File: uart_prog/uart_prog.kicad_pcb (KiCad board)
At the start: 2 copper layers, 22 parts, among them J1 USB_B_Micro, J2 Conn_01x06, Q1 MBT3904DW1, SW1 SW_SPDT, U1 FT231XQ

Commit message: Add pcb
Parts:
- moved R5 30.6 mm to (142.0, 80.0), turned to 180 degrees
- moved TP1 26.2 mm to (151.5, 77.5)
- moved TP2 25.7 mm to (156.5, 77.5)
- moved D1 23.5 mm to (146.3, 80.0), turned to 180 degrees
- moved R6 21.0 mm to (142.0, 77.5), turned to 180 degrees
- moved Q1 20.1 mm to (154.0, 82.0), turned to 270 degrees
- moved D2 19.2 mm to (146.3, 77.5), turned to 180 degrees
- moved C4 18.7 mm to (146.5, 85.0), turned to 180 degrees
- moved R3 17.6 mm to (151.5, 81.9), turned to 270 degrees
- moved R4 16.0 mm to (156.5, 81.9), turned to 90 degrees
- moved C5 14.0 mm to (153.1, 91.5)
- moved J2 11.3 mm to (167.0, 78.5)
- moved FB1 2.00 mm to (146.5, 83.0)
- moved F1 1.50 mm to (142.0, 83.0)

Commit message: Layout doner
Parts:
- removed TP1, TP2: TestPoint, TestPoint:TestPoint_THTPad_D2.0mm_Drill1.0mm
- C3: footprint Capacitor_SMD:C_01005_0402Metric -> Capacitor_SMD:C_0805_2012Metric_Pad1.18x1.45mm_HandSolder
- SW1: moved to B.Cu
- moved C3 19.9 mm to (146.5, 84.2)
- moved C4 10.9 mm to (157.0, 87.9), turned to 90 degrees
- moved C5 7.91 mm to (150.6, 84.0), turned to 180 degrees
- moved J2 6.75 mm to (160.2, 78.8)
- moved R3 6.21 mm to (157.6, 80.5), turned to 90 degrees
- moved R4 4.19 mm to (152.6, 80.5), turned to 270 degrees
- moved R5 2.37 mm to (142.7, 77.8)
- moved R6 2.37 mm to (142.7, 79.8)
- moved D2 2.27 mm to (146.5, 79.8)
- moved D1 2.26 mm to (146.5, 77.8)
- moved Q1 1.96 mm to (155.1, 80.3), turned to 90 degrees
- moved J1 1.75 mm to (136.8, 89.0)
- moved C1 1.58 mm to (143.5, 91.4)
- moved C2 1.58 mm to (143.5, 88.1)
- moved R1 1.58 mm to (146.1, 90.5)
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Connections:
- J1 pad 4: (no net) -> Net-(J1-Pad4)
- J2 pad 1: rx -> EN
- J2 pad 2: tx -> BOOT_OPT
- J2 pad 3: EN -> rx
- J2 pad 4: BOOT_OPT -> tx
- U1 pad 15: (no net) -> Net-(U1-Pad15)
- U1 pad 16: (no net) -> Net-(U1-Pad16)
- U1 pad 2: (no net) -> Net-(U1-Pad2)
- U1 pad 4: (no net) -> Net-(U1-Pad4)
- U1 pad 5: (no net) -> Net-(U1-Pad5)
- U1 pad 6: (no net) -> Net-(U1-Pad6)
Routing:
- net 5v: track 0.00 -> 36.5 mm, vias 0 -> 2
- net 3v3: track 0.00 -> 33.9 mm, vias 0 -> 2
- net vccio: track 0.00 -> 33.1 mm, vias 0 -> 2
- net GND: track 0.00 -> 27.3 mm, vias 0 -> 2
- net rxled: track 0.00 -> 20.4 mm, vias 0 -> 2
- net txled: track 0.00 -> 16.3 mm, vias 0 -> 2
- net rx: track 0.00 -> 15.0 mm, vias 0 -> 2
- net dtr: track 0.00 -> 14.6 mm, vias 0 -> 2
- net Net-(F1-Pad1): track 0.00 -> 8.41 mm, vias 0 -> 2
- net rts: track 0.00 -> 7.90 mm, vias 0 -> 2
- net tx: track 0.00 -> 7.73 mm
- net EN: track 0.00 -> 7.47 mm
- net /in2-: track 6.39 -> 12.4 mm
- net BOOT_OPT: track 0.00 -> 5.78 mm
- net /in2+: track 6.23 -> 11.2 mm
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- added copper zone on B.Cu, net GND
- added copper zone on F.Cu, net GND
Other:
- board outline added: 26.8 x 18.8 mm

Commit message: Pcb rev1
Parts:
- J1, J2: moved to B.Cu
- moved J2 12.8 mm to (160.2, 91.5)
- moved C1 3.54 mm to (143.0, 87.9), turned to 90 degrees
- moved C2 3.04 mm to (143.0, 91.1), turned to 270 degrees
- moved R1 1.90 mm to (145.4, 88.8)
- moved R2 1.46 mm to (145.4, 90.2)
- turned J1 to 90 degrees
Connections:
- J1 pad 4: Net-(J1-Pad4) -> (no net)
- J2 pad 1: EN -> GND
- J2 pad 2: BOOT_OPT -> 5v
- J2 pad 3: rx -> tx
- J2 pad 4: tx -> rx
- J2 pad 5: 5v -> BOOT_OPT
- J2 pad 6: GND -> EN
- U1 pad 15: Net-(U1-Pad15) -> (no net)
- U1 pad 16: Net-(U1-Pad16) -> (no net)
- U1 pad 2: Net-(U1-Pad2) -> (no net)
- U1 pad 4: Net-(U1-Pad4) -> (no net)
- U1 pad 5: Net-(U1-Pad5) -> (no net)
- U1 pad 6: Net-(U1-Pad6) -> (no net)
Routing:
- net Net-(F1-Pad1): track 8.41 -> 11.7 mm, vias 2 -> 1
- net /in2-: track 12.4 -> 9.76 mm, vias 2 -> 0
- net /in2+: track 11.2 -> 9.45 mm, vias 2 -> 0
- net vccio: track 33.1 -> 34.5 mm
- net /in+: track 6.99 -> 5.64 mm, vias 0 -> 1
- net dtr: track 14.6 -> 15.7 mm
- net 3v3: track 33.9 -> 33.1 mm
- net 5v: track 36.5 -> 37.3 mm
- net /in-: track 6.55 -> 5.78 mm, vias 0 -> 1
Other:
- board size 26.8 x 18.8 mm -> 26.8 x 17.5 mm
- board text added: "3v3"
- board text added: "5v"
- board text added: "EN BOOT RX TX 5V GND"

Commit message: Add schematic back again ...
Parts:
- D1, D2: footprint LED_SMD:LED_0805_2012Metric_Pad1.15x1.40mm_HandSolder -> LED_SMD:LED_0603_1608Metric_Pad1.05x0.95mm_HandSolder
- R5, R6: footprint Resistor_SMD:R_0805_2012Metric_Pad1.15x1.40mm_HandSolder -> Resistor_SMD:R_0603_1608Metric_Pad1.05x0.95mm_HandSolder
- moved R5 17.3 mm to (158.6, 84.7), turned to 0 degrees
- moved R6 16.2 mm to (158.6, 83.0), turned to 0 degrees
- moved SW1 11.6 mm to (146.4, 84.8), turned to 270 degrees
- moved C1 11.3 mm to (143.6, 76.6)
- moved C2 11.3 mm to (143.6, 79.8)
- moved R1 11.3 mm to (146.0, 77.5)
- moved R2 11.3 mm to (146.0, 79.0)
- moved D1 11.0 mm to (155.1, 84.7), turned to 0 degrees
- moved J1 10.3 mm to (137.0, 78.7)
- moved C4 9.28 mm to (149.6, 82.3), turned to 180 degrees
- moved D2 9.18 mm to (155.1, 83.0), turned to 0 degrees
- moved U1 8.81 mm to (150.9, 79.1), turned to 270 degrees
- moved C5 8.49 mm to (151.9, 75.6)
- moved R4 7.39 mm to (159.8, 79.3), turned to 90 degrees
- moved F1 4.99 mm to (138.5, 85.0)
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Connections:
- J2 pad 4: rx -> EN
- J2 pad 6: EN -> rx
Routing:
- net 3v3: track 33.1 -> 6.51 mm, vias 2 -> 0
- net rxled: track 20.4 -> 5.01 mm, vias 2 -> 0
- net dtr: track 15.7 -> 4.39 mm, vias 2 -> 0
- net 5v: track 37.3 -> 27.7 mm, vias 2 -> 0
- net /in2-: track 9.76 -> 2.40 mm
- net /in2+: track 9.45 -> 2.89 mm
- net GND: track 27.3 -> 20.8 mm, vias 2 -> 1
- net vccio: track 34.5 -> 30.5 mm
- net txled: track 16.2 -> 12.6 mm
- net tx: track 7.73 -> 10.9 mm
- net Net-(F1-Pad1): track 11.7 -> 8.91 mm
- net EN: track 7.47 -> 5.19 mm
- net rx: track 15.0 -> 13.0 mm, vias 2 -> 0
- net /in+: track 5.64 -> 6.73 mm
- net BOOT_OPT: track 5.78 -> 6.32 mm
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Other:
- board size 26.8 x 17.5 mm -> 28.6 x 16 mm
- board text added: "RX BOOT EN TX 5v GND"
- board text removed: "EN BOOT RX TX 5V GND"

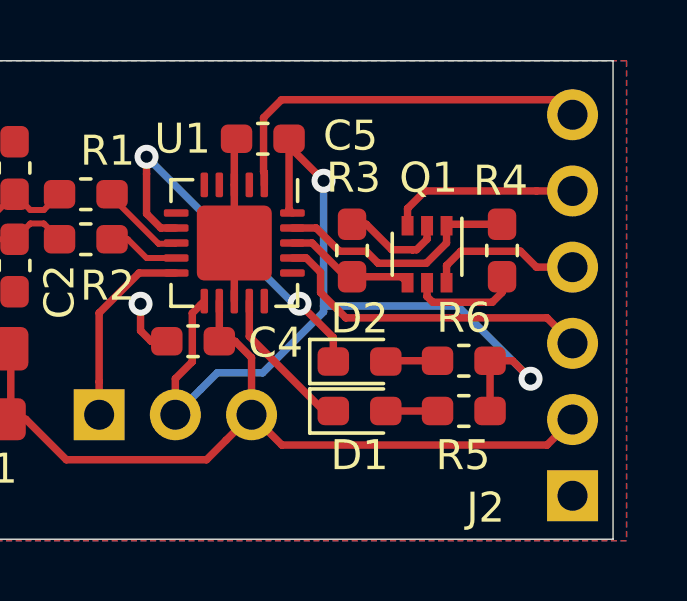
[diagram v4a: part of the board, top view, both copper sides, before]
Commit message: Updata schema to reflect board rev2
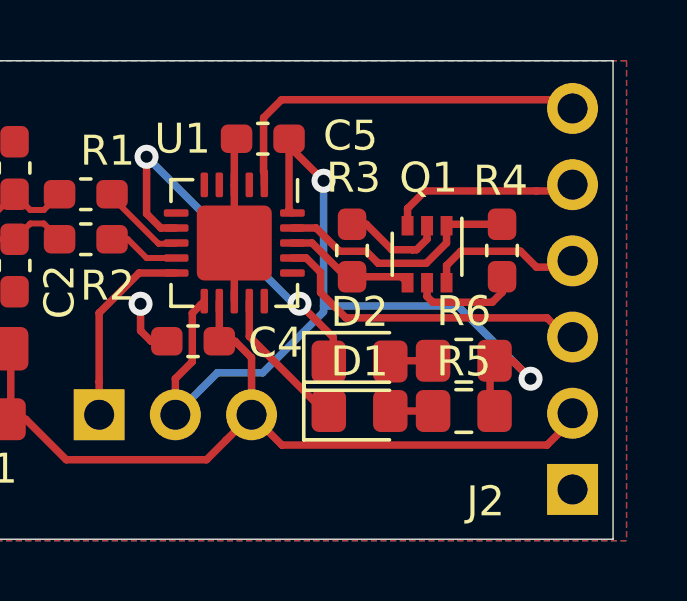
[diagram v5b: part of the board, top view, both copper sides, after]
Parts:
- D1, D2: footprint LED_SMD:LED_0603_1608Metric_Pad1.05x0.95mm_HandSolder -> LED_SMD:LED_0805_2012Metric_Pad1.15x1.40mm_HandSolder
- R5, R6: footprint Resistor_SMD:R_0603_1608Metric_Pad1.05x0.95mm_HandSolder -> Resistor_SMD:R_0805_2012Metric_Pad1.15x1.40mm_HandSolder
- moved J2 0.21 mm to (162.2, 87.3)
